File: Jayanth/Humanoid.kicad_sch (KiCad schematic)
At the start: 0 parts

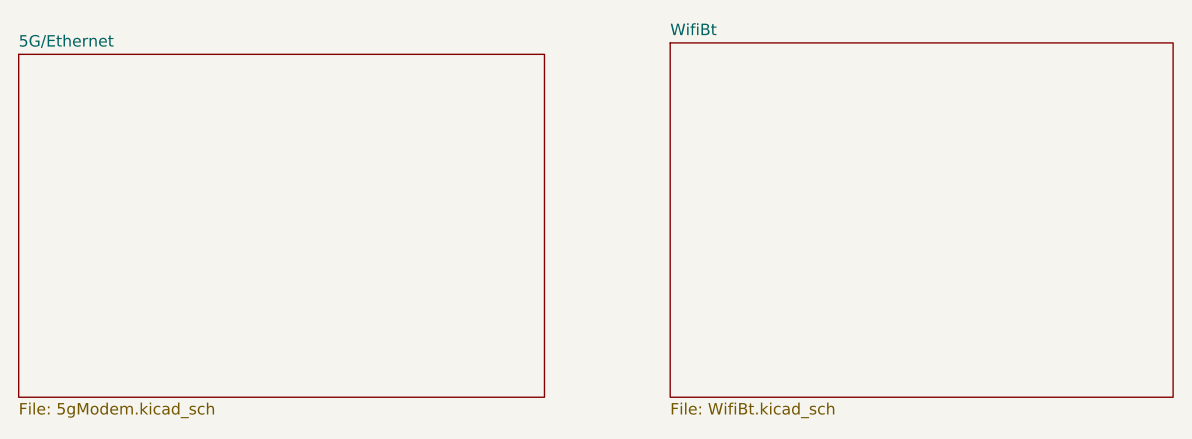
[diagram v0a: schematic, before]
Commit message: added can circuit
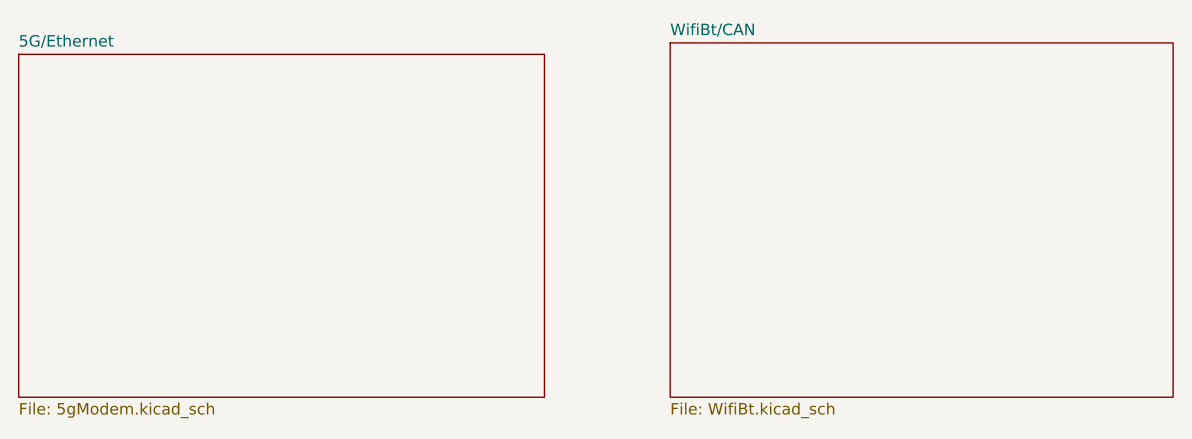
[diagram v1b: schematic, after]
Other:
- sheet WifiBt renamed WifiBt/CAN
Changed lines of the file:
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@@
 			(color 0 0 0 0.0000)
 		)
-		(property "Sheetname" "WifiBt"
+		(property "Sheetname" "WifiBt/CAN"
 			(at 92.71 17.0684 0)
 			(effects
